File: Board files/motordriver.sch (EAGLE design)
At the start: 13 parts, among them Q1 IPB034N03L, U1 VNH5019A

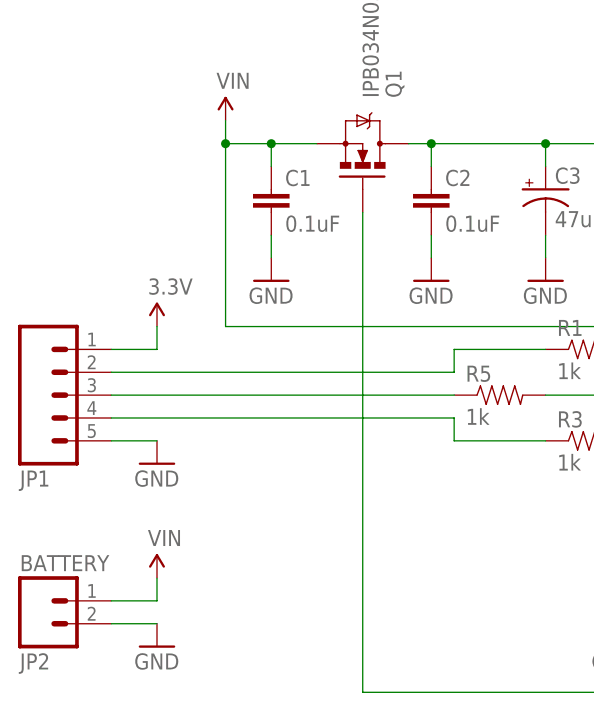
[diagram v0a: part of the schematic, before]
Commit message: Modified motor driver layout
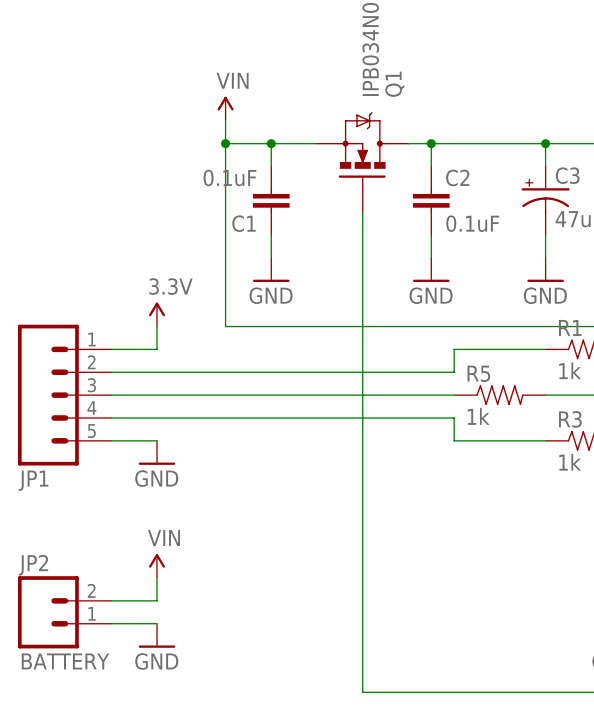
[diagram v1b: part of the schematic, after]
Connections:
- net GND: now also C1.1, JP2.1; no longer C1.2, JP2.2
- net VIN: now also C1.2, JP2.2; no longer C1.1, JP2.1
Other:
- moved on the sheet: C1, JP2
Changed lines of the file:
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@@
 <instances>
 <instance part="U1" gate="G$1" x="88.9" y="30.48"/>
-<instance part="JP2" gate="G$1" x="5.08" y="10.16" rot="MR180"/>
+<instance part="JP2" gate="G$1" x="5.08" y="7.62"/>
 <instance part="GND1" gate="1" x="17.78" y="25.4"/>
 <instance part="GND2" gate="1" x="17.78" y="5.08"/>
@@
 <instance part="SUPPLY3" gate="G$1" x="17.78" y="40.64"/>
 <instance part="SUPPLY4" gate="G$1" x="106.68" y="68.58"/>
-<instance part="C1" gate="G$1" x="30.48" y="53.34"/>
+<instance part="C1" gate="G$1" x="30.48" y="55.88" rot="R180"/>
 <instance part="C2" gate="G$1" x="48.26" y="53.34"/>
 <instance part="C3" gate="G$1" x="60.96" y="55.88"/>
@@
 <net name="GND" class="0">
 <segment>
-<pinref part="JP2" gate="G$1" pin="2"/>
+<pinref part="JP2" gate="G$1" pin="1"/>
 <wire x1="12.7" y1="7.62" x2="17.78" y2="7.62" width="0.1524" layer="91"/>
 <pinref part="GND2" gate="1" pin="GND"/>
@@
 </segment>
 <segment>
-<pinref part="C1" gate="G$1" pin="2"/>
+<pinref part="C1" gate="G$1" pin="1"/>
 <pinref part="GND4" gate="1" pin="GND"/>
 <wire x1="30.48" y1="50.8" x2="30.48" y2="48.26" width="0.1524" layer="91"/>
@@
 <net name="VIN" class="0">
 <segment>
-<pinref part="JP2" gate="G$1" pin="1"/>
+<pinref part="JP2" gate="G$1" pin="2"/>
 <wire x1="12.7" y1="10.16" x2="17.78" y2="10.16" width="0.1524" layer="91"/>
 <pinref part="SUPPLY2" gate="G$1" pin="VIN"/>
@@
 <wire x1="25.4" y1="40.64" x2="25.4" y2="60.96" width="0.1524" layer="91"/>
 <junction x="25.4" y="60.96"/>
-<pinref part="C1" gate="G$1" pin="1"/>
+<pinref part="C1" gate="G$1" pin="2"/>
 <wire x1="30.48" y1="58.42" x2="30.48" y2="60.96" width="0.1524" layer="91"/>
 <junction x="30.48" y="60.96"/>

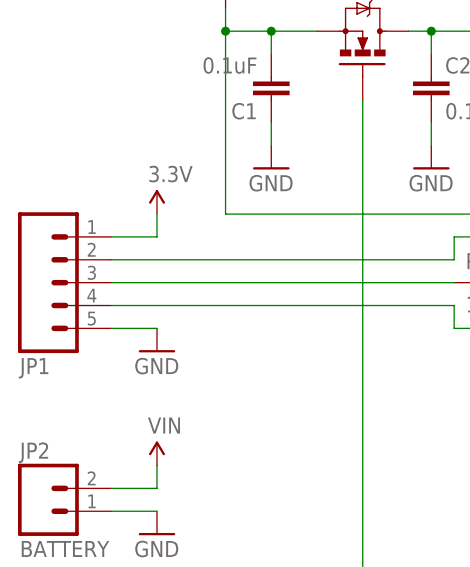
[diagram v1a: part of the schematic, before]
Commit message: Added labels and removed some thermals
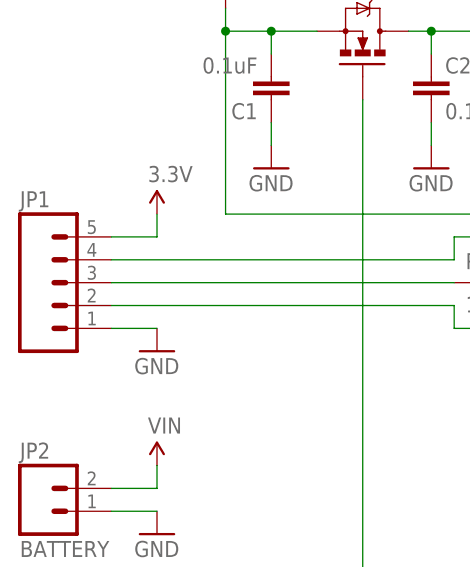
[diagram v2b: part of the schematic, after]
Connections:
- net 3.3V: now also JP1.5; no longer JP1.1
- net GND: now also JP1.1; no longer JP1.5
- net N$7: now also JP1.4; no longer JP1.2
- net N$8: now also JP1.2; no longer JP1.4
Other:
- moved on the sheet: JP1
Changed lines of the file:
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@@
 <instance part="GND1" gate="1" x="17.78" y="25.4"/>
 <instance part="GND2" gate="1" x="17.78" y="5.08"/>
-<instance part="JP1" gate="G$1" x="5.08" y="33.02" rot="MR180"/>
+<instance part="JP1" gate="G$1" x="5.08" y="33.02"/>
 <instance part="JP3" gate="G$1" x="124.46" y="38.1" rot="MR0"/>
 <instance part="Q1" gate="G$1" x="40.64" y="60.96" rot="MR90"/>
@@
 <pinref part="GND1" gate="1" pin="GND"/>
 <wire x1="12.7" y1="27.94" x2="17.78" y2="27.94" width="0.1524" layer="91"/>
-<pinref part="JP1" gate="G$1" pin="5"/>
+<pinref part="JP1" gate="G$1" pin="1"/>
 </segment>
 <segment>
@@
 <net name="3.3V" class="0">
 <segment>
-<pinref part="JP1" gate="G$1" pin="1"/>
+<pinref part="JP1" gate="G$1" pin="5"/>
 <wire x1="12.7" y1="38.1" x2="17.78" y2="38.1" width="0.1524" layer="91"/>
 <wire x1="17.78" y1="38.1" x2="17.78" y2="40.64" width="0.1524" layer="91"/>
@@
 <net name="N$7" class="0">
 <segment>
-<pinref part="JP1" gate="G$1" pin="2"/>
+<pinref part="JP1" gate="G$1" pin="4"/>
 <wire x1="12.7" y1="35.56" x2="50.8" y2="35.56" width="0.1524" layer="91"/>
 <wire x1="50.8" y1="35.56" x2="50.8" y2="38.1" width="0.1524" layer="91"/>
@@
 <net name="N$8" class="0">
 <segment>
-<pinref part="JP1" gate="G$1" pin="4"/>
+<pinref part="JP1" gate="G$1" pin="2"/>
 <wire x1="12.7" y1="30.48" x2="50.8" y2="30.48" width="0.1524" layer="91"/>
 <wire x1="50.8" y1="30.48" x2="50.8" y2="27.94" width="0.1524" layer="91"/>

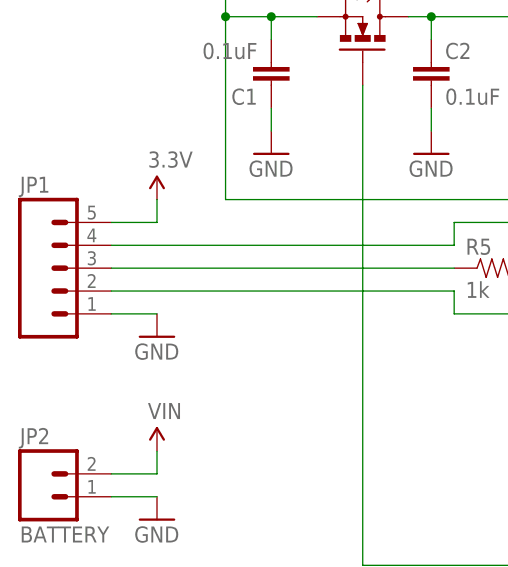
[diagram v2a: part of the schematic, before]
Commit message: Switched to polarized connectors
Also added 3.3v out pins on logic board, various other changes
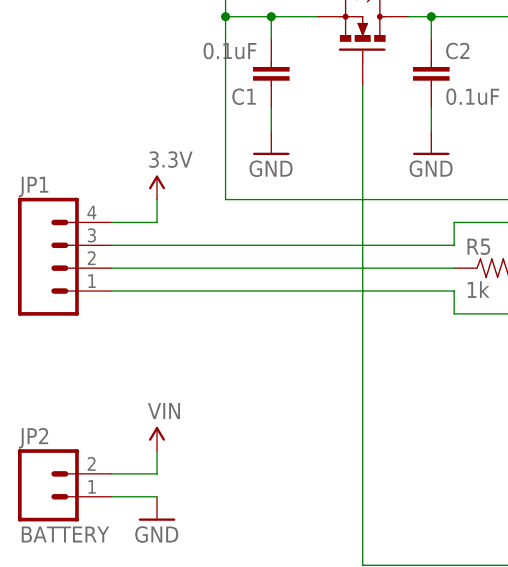
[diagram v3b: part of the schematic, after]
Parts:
- JP1: device SparkFun-Connectors:M05LOCK_LONGPADS -> SparkFun-Connectors:M04POLAR_LOCK
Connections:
- net 3.3V: now also JP1.4; no longer JP1.5
- net GND: no longer JP1.1
- net N$5: now also JP1.2; no longer JP1.3
- net N$7: now also JP1.3; no longer JP1.4
- net N$8: now also JP1.1; no longer JP1.2
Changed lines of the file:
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@@
 <part name="U1" library="Custom" deviceset="VNH5019A" device=""/>
 <part name="JP2" library="SparkFun-Connectors" deviceset="M02" device="5MM" value="BATTERY"/>
-<part name="GND1" library="SparkFun-Aesthetics" deviceset="GND" device=""/>
 <part name="GND2" library="SparkFun-Aesthetics" deviceset="GND" device=""/>
-<part name="JP1" library="SparkFun-Connectors" deviceset="M05" device="LOCK_LONGPADS"/>
 <part name="JP3" library="SparkFun-Connectors" deviceset="M02" device="5MM" value="MOTOR"/>
 <part name="Q1" library="SparkFun-DiscreteSemi" deviceset="MOSFET-NCHANNEL" device="FDD8780" value="IPB034N03L"/>
@@
 <part name="GND5" library="SparkFun-Aesthetics" deviceset="GND" device=""/>
 <part name="GND6" library="SparkFun-Aesthetics" deviceset="GND" device=""/>
+<part name="JP1" library="SparkFun-Connectors" deviceset="M04" device="POLAR_LOCK"/>
 </parts>
 <sheets>
@@
 <instance part="U1" gate="G$1" x="88.9" y="30.48"/>
 <instance part="JP2" gate="G$1" x="5.08" y="7.62"/>
-<instance part="GND1" gate="1" x="17.78" y="25.4"/>
 <instance part="GND2" gate="1" x="17.78" y="5.08"/>
-<instance part="JP1" gate="G$1" x="5.08" y="33.02"/>
 <instance part="JP3" gate="G$1" x="124.46" y="38.1" rot="MR0"/>
 <instance part="Q1" gate="G$1" x="40.64" y="60.96" rot="MR90"/>
@@
 <instance part="GND5" gate="1" x="48.26" y="45.72"/>
 <instance part="GND6" gate="1" x="60.96" y="45.72"/>
+<instance part="JP1" gate="G$1" x="7.62" y="33.02"/>
 </instances>
 <busses>
@@
 <wire x1="12.7" y1="7.62" x2="17.78" y2="7.62" width="0.1524" layer="91"/>
 <pinref part="GND2" gate="1" pin="GND"/>
-</segment>
-<segment>
-<pinref part="GND1" gate="1" pin="GND"/>
-<wire x1="12.7" y1="27.94" x2="17.78" y2="27.94" width="0.1524" layer="91"/>
-<pinref part="JP1" gate="G$1" pin="1"/>
 </segment>
 <segment>
@@
 <net name="3.3V" class="0">
 <segment>
-<pinref part="JP1" gate="G$1" pin="5"/>
 <wire x1="12.7" y1="38.1" x2="17.78" y2="38.1" width="0.1524" layer="91"/>
 <wire x1="17.78" y1="38.1" x2="17.78" y2="40.64" width="0.1524" layer="91"/>
 <pinref part="SUPPLY3" gate="G$1" pin="3.3V"/>
+<pinref part="JP1" gate="G$1" pin="4"/>
 </segment>
 <segment>
@@
 <segment>
 <pinref part="R5" gate="G$1" pin="1"/>
-<pinref part="JP1" gate="G$1" pin="3"/>
 <wire x1="50.8" y1="33.02" x2="12.7" y2="33.02" width="0.1524" layer="91"/>
+<pinref part="JP1" gate="G$1" pin="2"/>
 </segment>
 </net>
 <net name="N$7" class="0">
 <segment>
-<pinref part="JP1" gate="G$1" pin="4"/>
 <wire x1="12.7" y1="35.56" x2="50.8" y2="35.56" width="0.1524" layer="91"/>
 <wire x1="50.8" y1="35.56" x2="50.8" y2="38.1" width="0.1524" layer="91"/>
 <pinref part="R1" gate="G$1" pin="1"/>
 <wire x1="50.8" y1="38.1" x2="60.96" y2="38.1" width="0.1524" layer="91"/>
+<pinref part="JP1" gate="G$1" pin="3"/>
 </segment>
 </net>
 <net name="N$8" class="0">
 <segment>
-<pinref part="JP1" gate="G$1" pin="2"/>
 <wire x1="12.7" y1="30.48" x2="50.8" y2="30.48" width="0.1524" layer="91"/>
 <wire x1="50.8" y1="30.48" x2="50.8" y2="27.94" width="0.1524" layer="91"/>
 <pinref part="R3" gate="G$1" pin="1"/>
 <wire x1="50.8" y1="27.94" x2="60.96" y2="27.94" width="0.1524" layer="91"/>
-</segment>
-</net>
+<pinref part="JP1" gate="G$1" pin="1"/>
+</segment>
+</net>

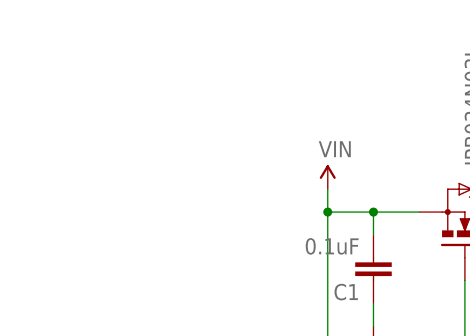
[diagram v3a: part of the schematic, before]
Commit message: Modified boards to facilitate mounting
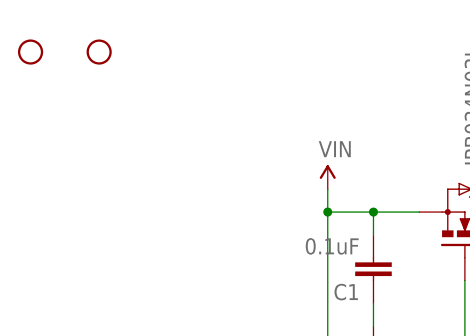
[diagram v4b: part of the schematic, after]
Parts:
- added STANDOFF1, STANDOFF2: STAND-OFF, SparkFun-Electromechanical:STAND-OFF
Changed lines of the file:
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@@
 <part name="GND6" library="SparkFun-Aesthetics" deviceset="GND" device=""/>
 <part name="JP1" library="SparkFun-Connectors" deviceset="M04" device="POLAR_LOCK"/>
+<part name="STANDOFF1" library="SparkFun-Electromechanical" deviceset="STAND-OFF" device=""/>
+<part name="STANDOFF2" library="SparkFun-Electromechanical" deviceset="STAND-OFF" device=""/>
 </parts>
 <sheets>
@@
 <instance part="GND6" gate="1" x="60.96" y="45.72"/>
 <instance part="JP1" gate="G$1" x="7.62" y="33.02"/>
+<instance part="STANDOFF1" gate="G$1" x="-7.62" y="78.74"/>
+<instance part="STANDOFF2" gate="G$1" x="0" y="78.74"/>
 </instances>
 <busses>
